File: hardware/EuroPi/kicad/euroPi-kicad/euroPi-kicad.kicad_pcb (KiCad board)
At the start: 2 copper layers, 121.9 x 128.5 mm, 95 parts, among them J1 Output 1 Jack, J10 Eurorack Power 2x8 16p, J11 Conn_01x13_Socket, J12 OLED 64x128, J13 USB_B_Micro, J14 Conn_01x03_Pin, J15 Conn_01x04_Pin, J16 Conn_02x04_Top_Bottom, J17 Conn_01x13_Pin, J18 Conn_01x04_Pin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

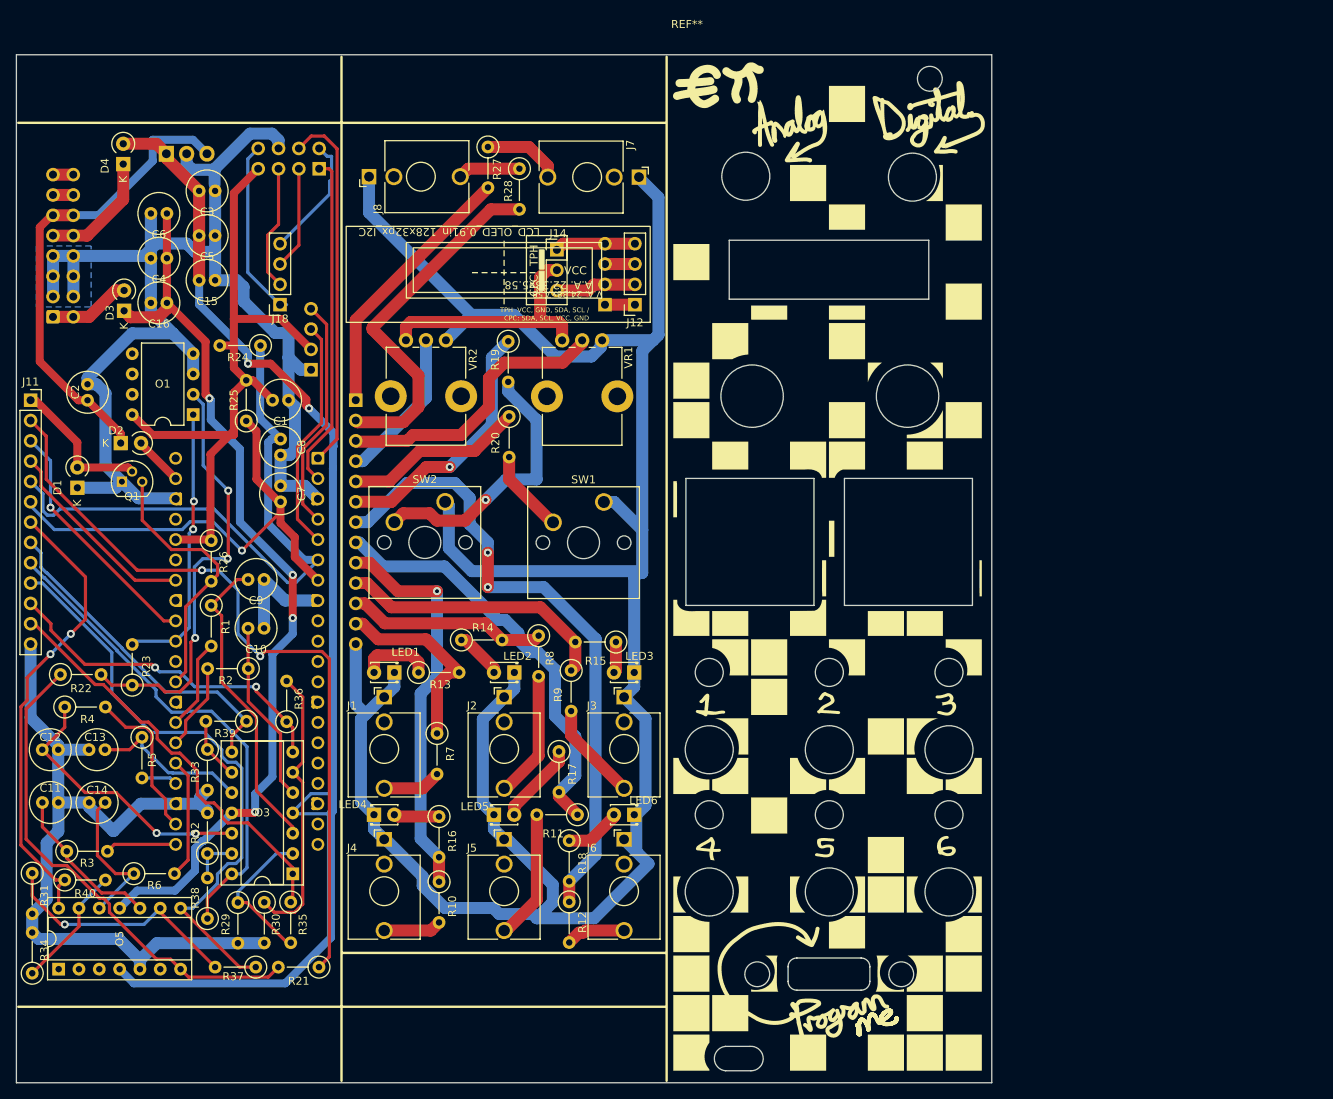
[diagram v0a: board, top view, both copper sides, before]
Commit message: further cleaning rearranging boards to make it easier to score for seperation
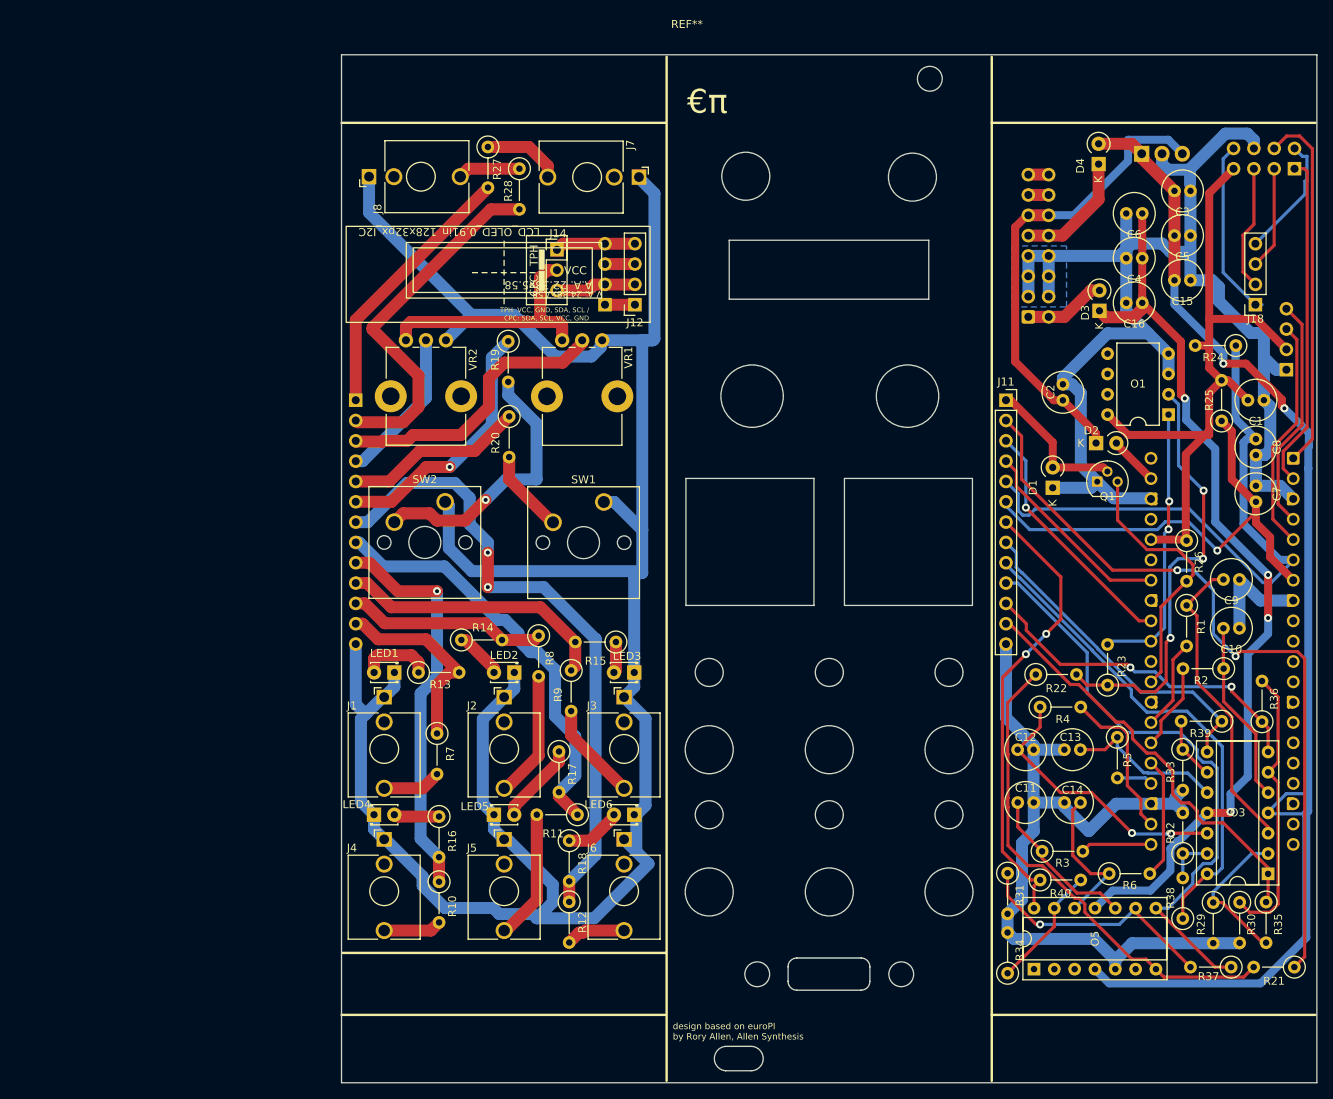
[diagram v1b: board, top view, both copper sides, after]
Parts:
- moved C1 121.9 mm to (194.6, 68.6)
- moved C13 121.9 mm to (173.6, 112.3)
- moved C16 121.9 mm to (179.4, 56.4)
- moved C4 121.9 mm to (179.4, 50.8)
- moved C6 121.9 mm to (179.4, 45.2)
- moved C7 121.9 mm to (195.6, 81.3)
- moved C8 121.9 mm to (195.6, 73.4)
- moved D1 121.9 mm to (170.2, 79.5)
- moved D2 121.9 mm to (175.6, 73.9)
- moved O3 121.9 mm to (197.1, 127.8)
- moved R23 121.9 mm to (177.0, 104.2)
- moved R29 121.9 mm to (190.2, 131.4)
- moved R31 121.9 mm to (164.5, 127.7)
- moved R34 121.9 mm to (164.5, 140.2)
- moved R36 121.9 mm to (196.3, 108.8)
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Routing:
- net CJ6: track 137.2 -> 136.6 mm
- net Net-(O5-Pad7): track 62.1 -> 61.5 mm
- net I2C_GND: track 577.9 -> 577.3 mm
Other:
- outline, holes or cut-outs redrawn
- board text added: "design based on euroPI by Rory Allen, Allen Synthesis"
- board text added: "€π"
- board text added: "€π FRONT PANEL BACK v1.0"
- board text added: "€π MAIN PANEL BACK v1.0"
- board text added: "€π UI PANEL BACK v1.0"

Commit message: cosmetics fixes and trardrops
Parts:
- moved J13 1.65 mm to (142.2, 142.0)
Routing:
- net Net-(O3D-+): track 34.6 -> 35.2 mm
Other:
- outline, holes or cut-outs redrawn
- board text added: "-PICO"
- board text added: "1"
- board text added: "2"
- board text added: "3"
- board text added: "4"
- board text added: "5"
- board text added: "6"
- board text added: "ANALOG IN"
- board text added: "DIGITAL IN"
- board text added: "PROGRAM ME!!"
- board text added: "π"
- board text added: "€"
- board text removed: "€π"
